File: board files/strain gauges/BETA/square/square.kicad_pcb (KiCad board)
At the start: 2 copper layers, 40 x 40 mm, 10 parts, among them J1 PR&J

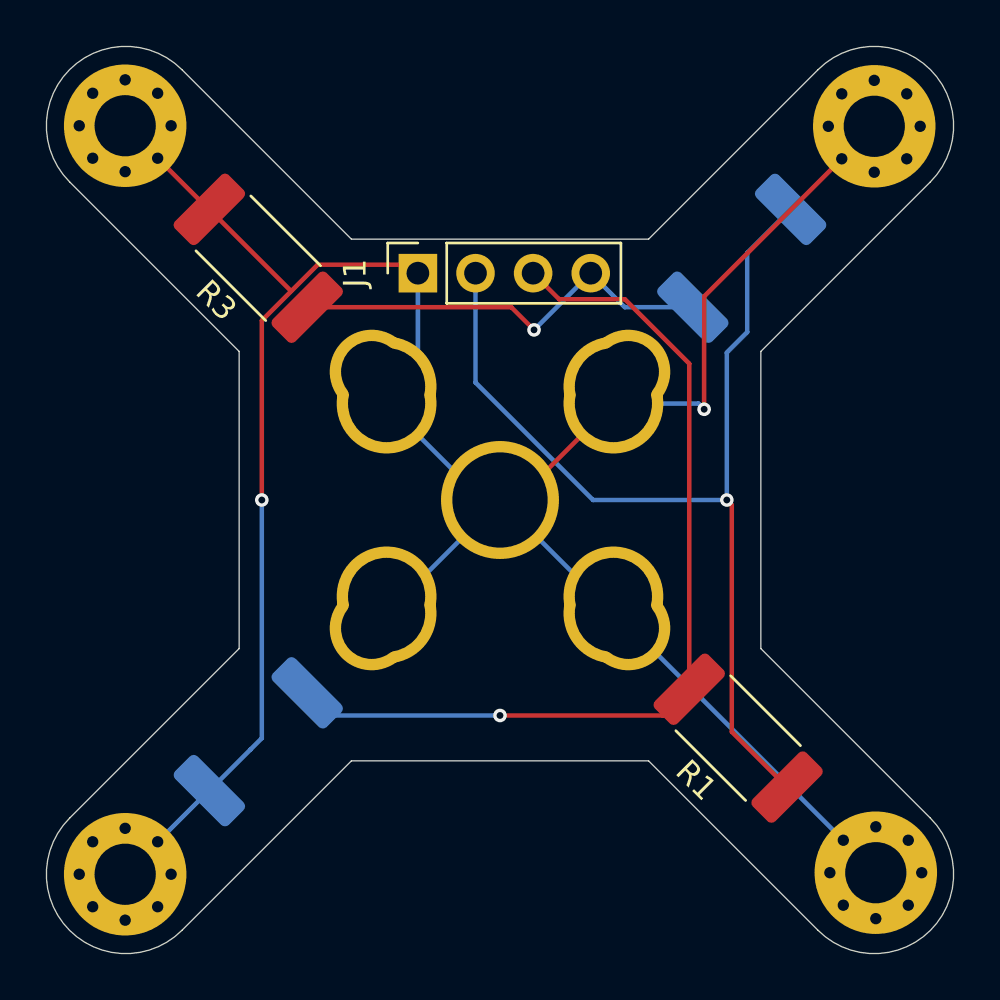
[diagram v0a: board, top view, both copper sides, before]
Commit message: added PRJ logo to strain gauge boards
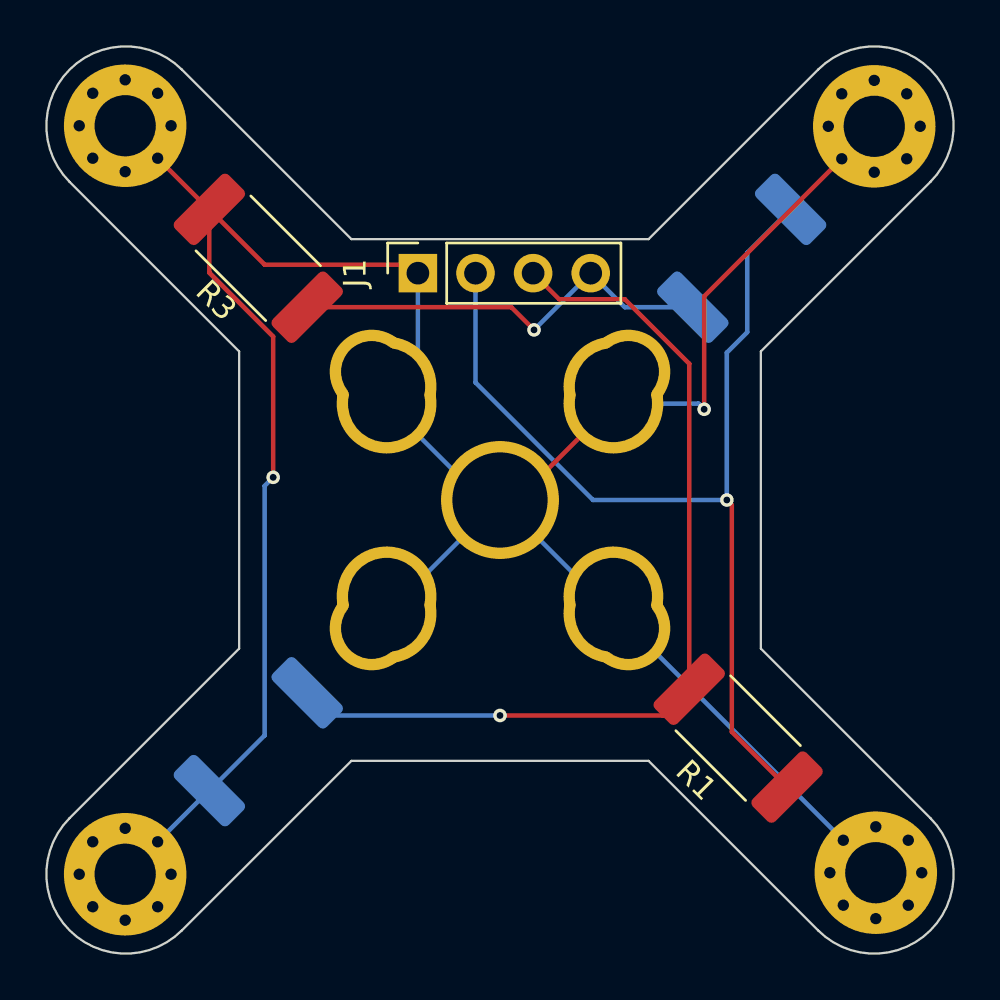
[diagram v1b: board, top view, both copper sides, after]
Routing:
- net GND: track 114.9 -> 118.4 mm
